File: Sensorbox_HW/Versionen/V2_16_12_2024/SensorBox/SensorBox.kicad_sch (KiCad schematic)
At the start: 28 parts, among them J1 SD_Card, Q1 NPN, U1 BME280, U2 PS1-O3-100, U3 Beetle ESP32-C6, U6 TPS629211QDRLRQ1, U8 HPP845E131R5

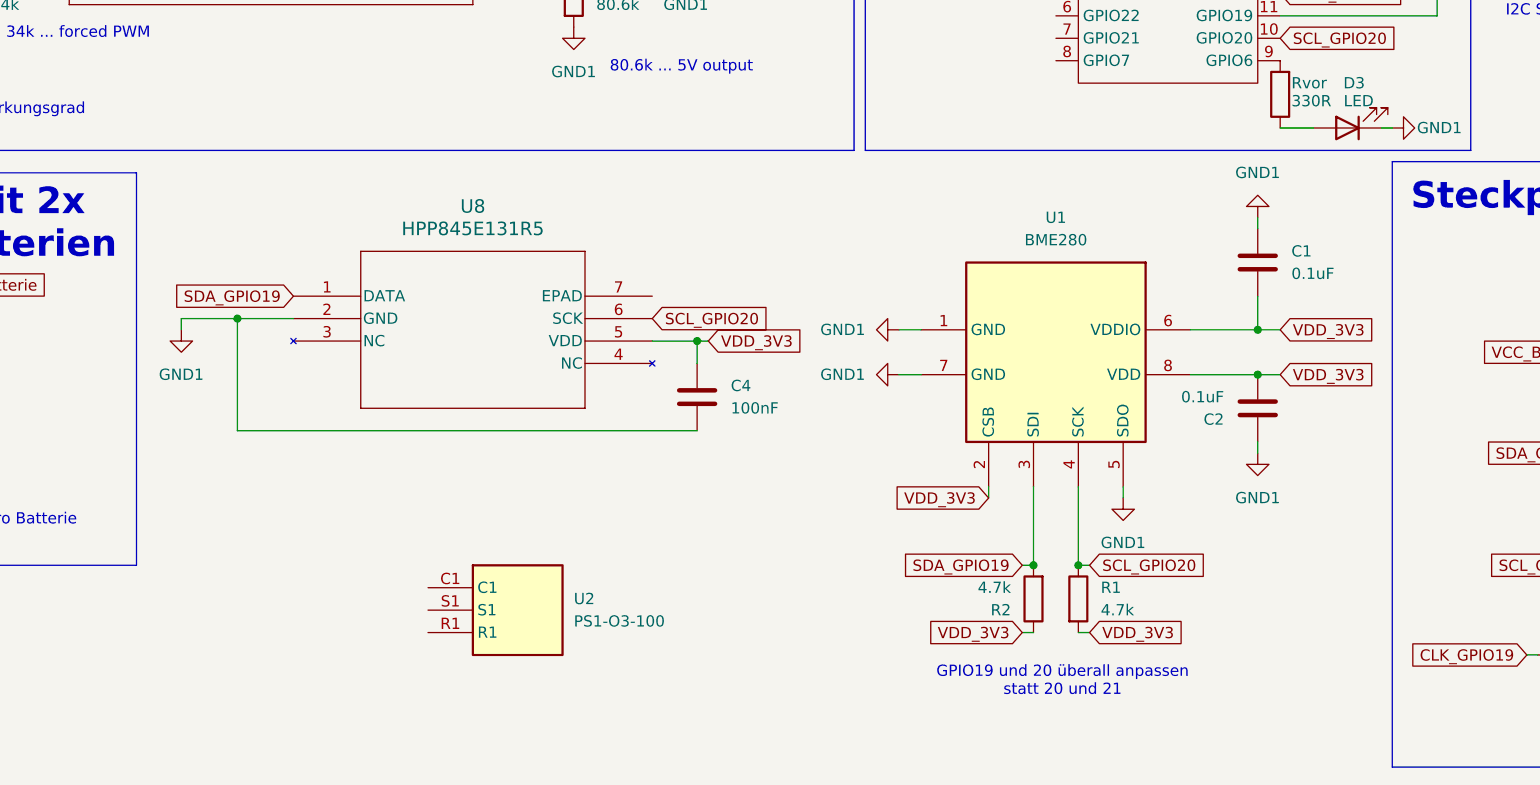
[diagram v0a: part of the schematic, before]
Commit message: änderung schaltplan (Anordnung)
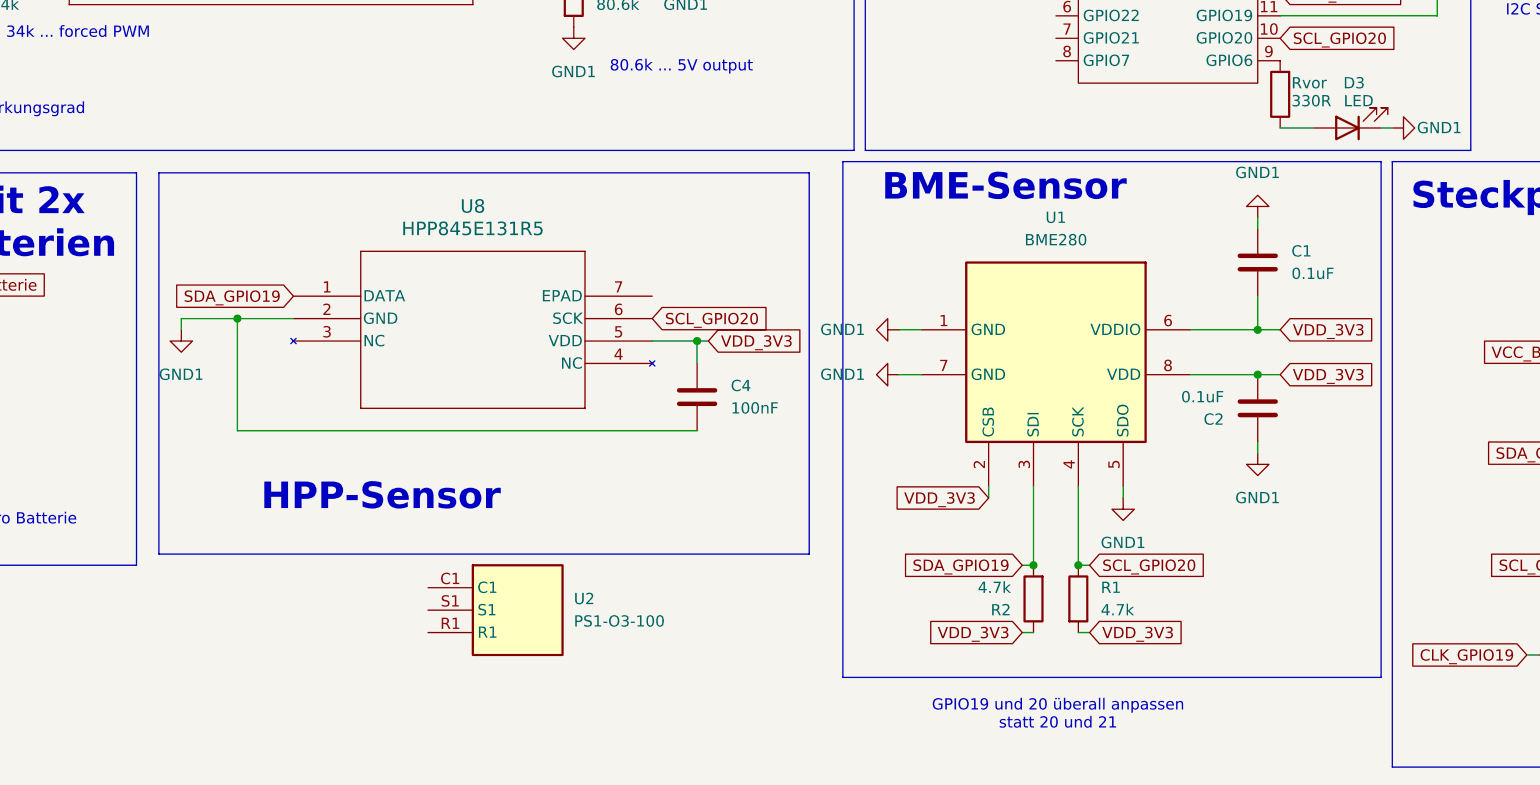
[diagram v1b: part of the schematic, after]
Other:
- note added: "BME-Sensor"
- note added: "HPP-Sensor"
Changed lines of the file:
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@@
+	)
+	(rectangle
+		(start 54.61 82.55)
+		(end 128.27 125.73)
+		(stroke
+			(width 0)
+			(type default)
+		)
+		(fill
+			(type none)
+		)
 	)
 	(rectangle
@@
 		(start 134.62 15.24)
 		(end 203.2 80.01)
+		(stroke
+			(width 0)
+			(type default)
+		)
+		(fill
+			(type none)
+		)
+	)
+	(rectangle
+		(start 132.08 81.28)
+		(end 193.04 139.7)
 		(stroke
 			(width 0)
@@
 		)
 	)
+	(text "BME-Sensor\n"
+		(exclude_from_sim no)
+		(at 150.368 84.328 0)
+		(effects
+			(font
+				(size 3 3)
+				(thickness 0.6)
+				(bold yes)
+			)
+		)
+	)
 	(text "Memory-Card\n"
 		(exclude_from_sim no)
@@
 		)
 	)
+	(text "HPP-Sensor\n"
+		(exclude_from_sim no)
+		(at 79.756 119.38 0)
+		(effects
+			(font
+				(size 3 3)
+				(thickness 0.6)
+				(bold yes)
+			)
+		)
+	)
 	(text "1A 95% Wirkungsgrad\n"
 		(exclude_from_sim no)
@@
 	(text "GPIO19 und 20 überall anpassen\nstatt 20 und 21\n"
 		(exclude_from_sim no)
-		(at 156.972 140.208 0)
+		(at 156.464 144.018 0)
 		(effects
 			(font
